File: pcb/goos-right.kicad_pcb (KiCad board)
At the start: 2 copper layers, 140.2 x 108.1 mm, 22 parts

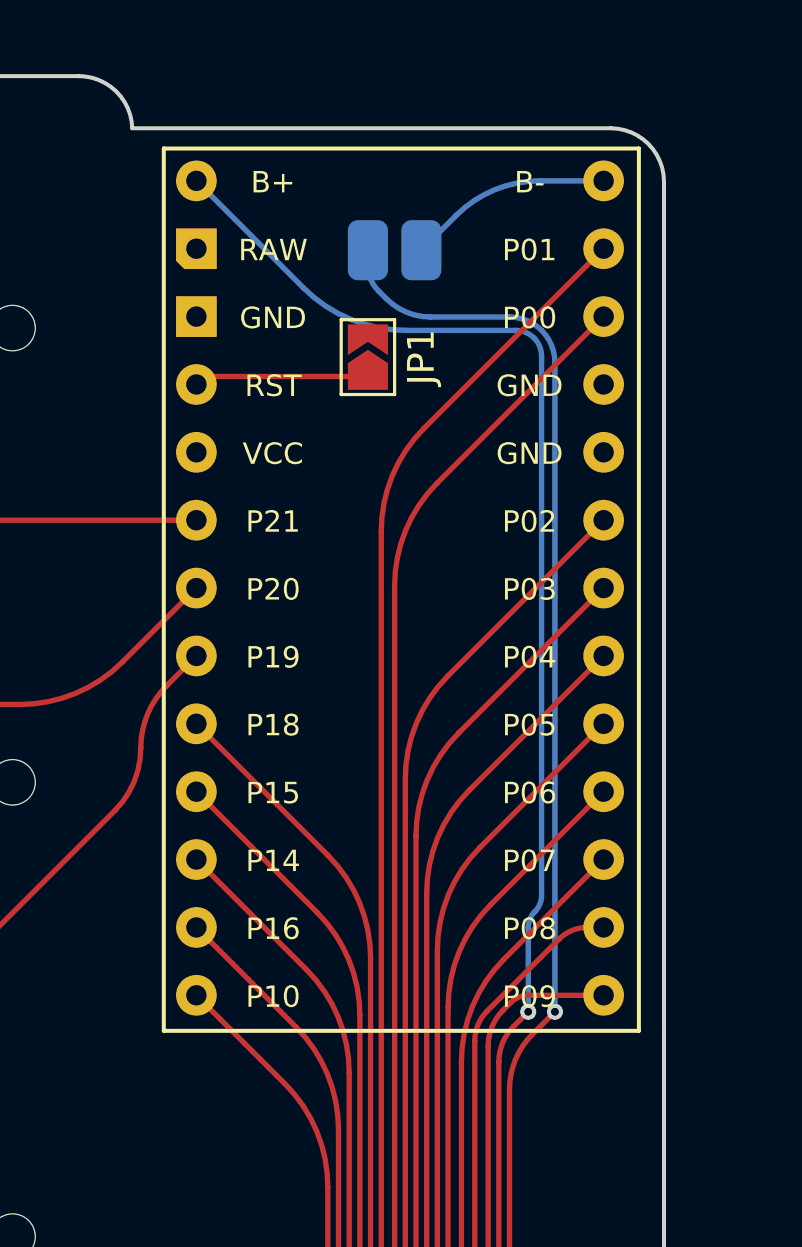
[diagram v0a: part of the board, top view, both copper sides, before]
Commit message: feat: added github text
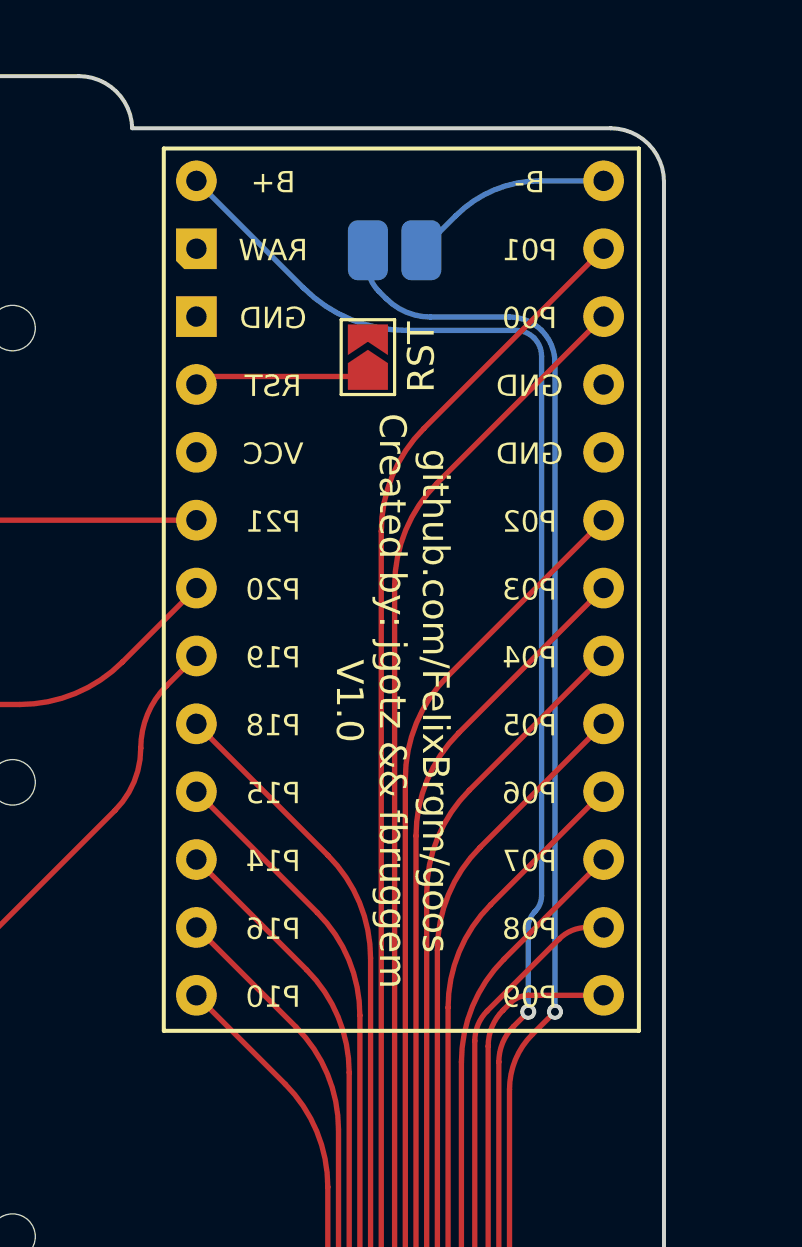
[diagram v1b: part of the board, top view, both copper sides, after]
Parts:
- renumbered JP1 to RST
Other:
- board text added: "github.com/FelixBrgm/goos Created by: jgotz && fbruggem V1.0"

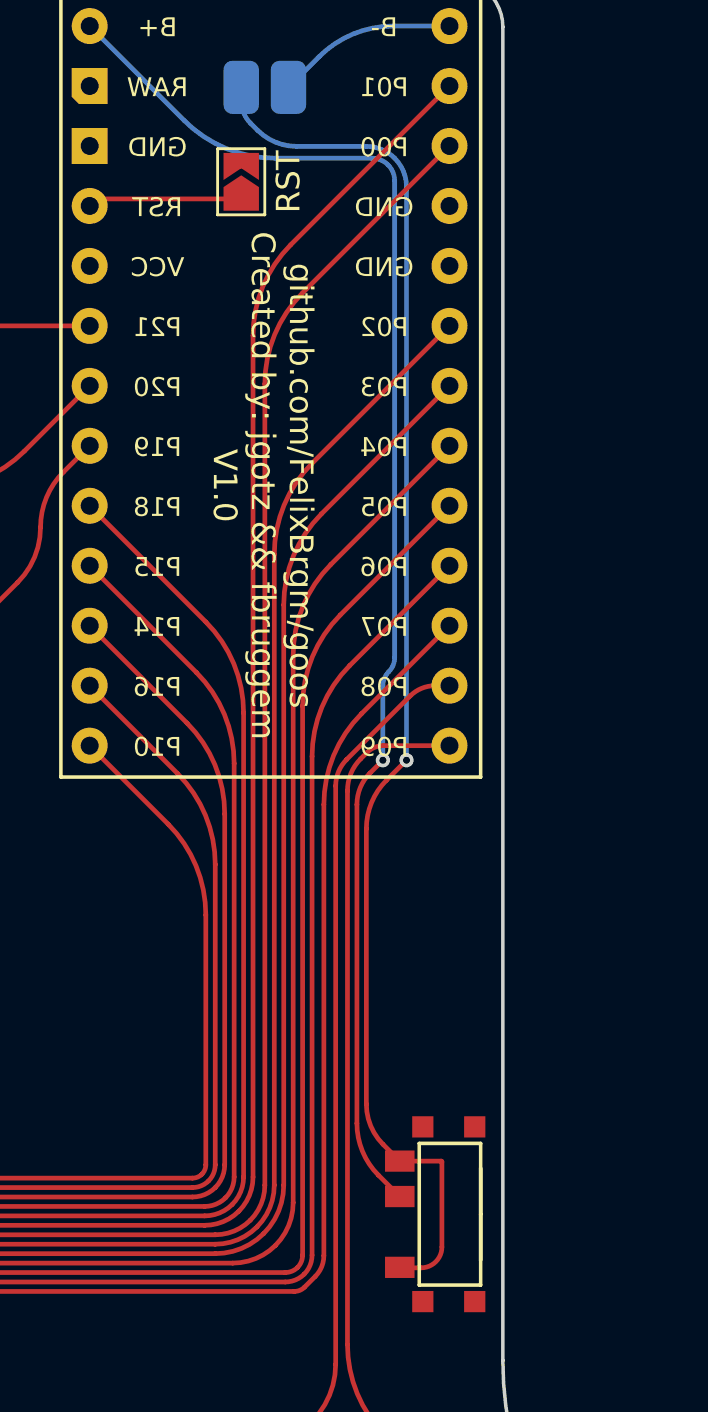
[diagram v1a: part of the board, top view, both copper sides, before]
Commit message: fix: switch being permanently on
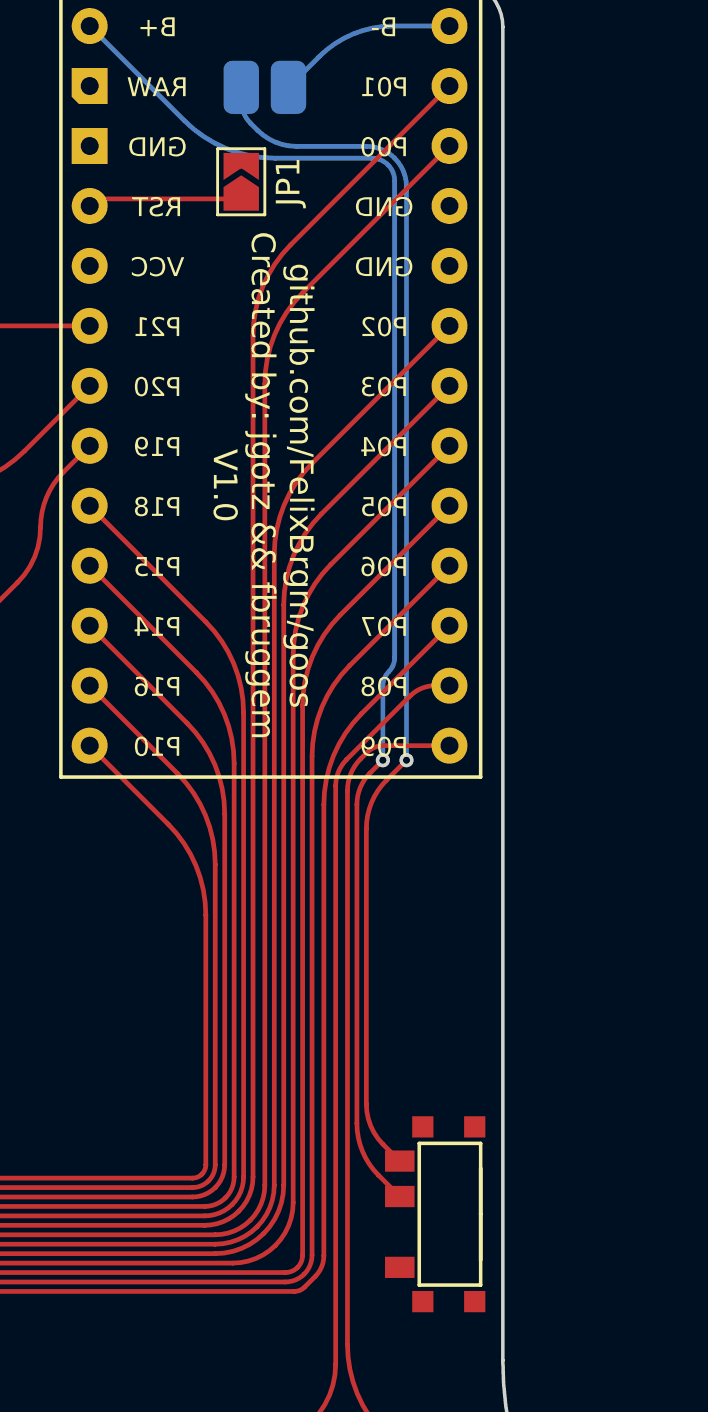
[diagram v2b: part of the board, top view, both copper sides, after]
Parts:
- renumbered RST to JP1
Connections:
- S1 pad 1: Net-(J1-B+) -> unconnected-(S1-SW-Pad1)
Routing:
- net Net-(J1-B+): track 59.4 -> 51.8 mm
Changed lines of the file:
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@@
 			(outputformat 1)
 			(mirror no)
-			(drillshape 1)
+			(drillshape 0)
 			(scaleselection 1)
-			(outputdirectory "")
+			(outputdirectory "../../gerbers/")
 		)
 	)
@@
 	(net 24 "unconnected-(U1-RAW-Pad15)")
 	(net 25 "unconnected-(U1-VCC-Pad18)")
+	(net 26 "unconnected-(S1-SW-Pad1)")
 	(footprint "Jumper:SolderJumper-2_P1.3mm_Open_TrianglePad1.0x1.5mm"
 		(layer "F.Cu")
@@
 		(descr "SMD Solder Jumper, 1x1.5mm Triangular Pads, 0.3mm gap, open")
 		(tags "solder jumper open")
-		(property "Reference" "RST"
-			(at 0 2 270)
+		(property "Reference" "JP1"
+			(at 0 2 -90)
 			(layer "F.SilkS")
 			(effects
@@
 		)
 		(pad "" np_thru_hole circle
-			(at -5.000002 -3.75 348)
+			(at -5.000003 -3.75 348)
 			(size 3 3)
 			(drill 3)
@@
 		)
 		(pad "" np_thru_hole circle
-			(at -5.000002 -3.75 348)
+			(at -5.000003 -3.75 348)
 			(size 3 3)
 			(drill 3)
@@
 			(size 0.9 1.25)
 			(layers "F.Cu" "F.Paste" "F.Mask")
-			(net 1 "Net-(J1-B+)")
+			(net 26 "unconnected-(S1-SW-Pad1)")
 			(pinfunction "SW")
-			(pintype "passive")
+			(pintype "passive+no_connect")
 		)
 		(pad "2" smd rect
@@
 		)
 		(pad "" np_thru_hole circle
-			(at -5.000002 -3.75 348)
+			(at -5.000003 -3.75 348)
 			(size 3 3)
 			(drill 3)
@@
 			)
 		)
+		(sheetname "Root")
+		(sheetfile "goos-right.kicad_sch")
 		(attr through_hole)
 		(fp_line
@@
 	)
 	(segment
-		(start 241.725681 85.489849)
-		(end 241.715531 85.479699)
-		(width 0.2)
-		(layer "F.Cu")
-		(net 1)
-	)
-	(segment
-		(start 243.465344 80.979699)
-		(end 241.715531 80.979699)
-		(width 0.2)
-		(layer "F.Cu")
-		(net 1)
-	)
-	(segment
-		(start 241.750186 85.5)
-		(end 242.617916 85.5)
-		(width 0.2)
-		(layer "F.Cu")
-		(net 1)
-	)
-	(segment
 		(start 240.3 78.563236)
 		(end 240.3 66.902081)
@@
 	)
 	(segment
-		(start 243.5 84.617916)
-		(end 243.5 81.014354)
-		(width 0.2)
-		(layer "F.Cu")
-		(net 1)
-	)
-	(segment
 		(start 241.007765 80.271933)
 		(end 241.715531 80.979699)
@@
 	)
 	(arc
-		(start 243.5 84.617916)
-		(mid 243.241643 85.241643)
-		(end 242.617916 85.5)
-		(width 0.2)
-		(layer "F.Cu")
-		(net 1)
-	)
-	(arc
-		(start 243.489849 80.989849)
-		(mid 243.497361 81.001092)
-		(end 243.5 81.014354)
-		(width 0.2)
-		(layer "F.Cu")
-		(net 1)
-	)
-	(arc
-		(start 243.489849 80.989849)
-		(mid 243.478606 80.982336)
-		(end 243.465344 80.979699)
-		(width 0.2)
-		(layer "F.Cu")
-		(net 1)
-	)
-	(arc
 		(start 240.3 78.563236)
 		(mid 240.483942 79.487976)
@@
 	)
 	(arc
-		(start 241.725681 85.489849)
-		(mid 241.736924 85.497361)
-		(end 241.750186 85.5)
-		(width 0.2)
-		(layer "F.Cu")
-		(net 1)
-	)
-	(arc
 		(start 241.15 64.85)
 		(mid 240.520907 65.791502)
@@
 		(net 23)
 	)
+	(segment
+		(start 241.725681 85.489849)
+		(end 241.715531 85.479699)
+		(width 0.2)
+		(layer "F.Cu")
+		(net 26)
+	)
+	(arc
+		(start 241.725681 85.489849)
+		(mid 241.736924 85.497361)
+		(end 241.750186 85.5)
+		(width 0.2)
+		(layer "F.Cu")
+		(net 26)
+	)
 	(zone

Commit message: feat: fixed right half
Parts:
- removed JP1: SolderJumper_2_Open, Jumper:SolderJumper-2_P1.3mm_Open_TrianglePad1.0x1.5mm
- added RST: SolderJumper_2_Open, Jumper:SolderJumper-2_P1.3mm_Open_TrianglePad1.0x1.5mm, F.Cu at (-82.5, 59.0)
- U1: moved to F.Cu
- moved S1 320.0 mm to (-75.5, 103.2)
- moved S2 319.3 mm to (-183.9, 81.8)
- moved S5 319.2 mm to (-165.5, 59.0)
- moved S13 318.9 mm to (-121.0, 91.7)
- moved S8 318.9 mm to (-143.9, 49.5)
- moved S16 318.9 mm to (-102.0, 94.4)
- moved S10 318.9 mm to (-140.6, 87.7)
- moved S19 318.8 mm to (-68.1, 136.5)
- moved S3 318.8 mm to (-178.3, 100.2)
- moved S17 318.8 mm to (-102.5, 116.6)
- moved S6 318.8 mm to (-162.1, 77.7)
- moved S9 318.8 mm to (-142.2, 68.6)
- moved S12 318.8 mm to (-121.0, 72.5)
- moved S15 318.8 mm to (-102.0, 75.4)
- moved S18 318.8 mm to (-84.0, 124.3)
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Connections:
- S1 pad 1: unconnected-(S1-SW-Pad1) -> Net-(J1-B+)
- S1 pad 3: Net-(J1-B+) -> unconnected-(S1-SW-Pad3)
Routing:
- net D9: track 50.8 -> 105.8 mm
- net D8: track 44.7 -> 86.8 mm
- net D20: track 23.4 -> 52.8 mm
- net D21: track 29.6 -> 58.1 mm
- net D16: track 95.8 -> 75.4 mm, vias 0 -> 2
- net D10: track 109.4 -> 89.4 mm, vias 0 -> 2
- net D19: track 28.9 -> 46.3 mm, vias 0 -> 2
- net D14: track 82.5 -> 67.5 mm, vias 0 -> 2
- net D1: track 137.1 -> 123.2 mm
- net D3: track 134.0 -> 120.8 mm
- net D5: track 144.7 -> 134.2 mm
- net D4: track 161.3 -> 150.9 mm
- net D7: track 61.2 -> 51.4 mm
- net D6: track 138.2 -> 128.7 mm
- net D2: track 151.2 -> 141.7 mm
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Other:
- board size 140.2 x 108.1 mm -> 142.9 x 112.6 mm
- board text added: "github.com/FelixBrgm/goos Created by: jgotz && fbruggem V0.0.1"
- board text removed: "github.com/FelixBrgm/goos Created by: jgotz && fbruggem V1.0"
